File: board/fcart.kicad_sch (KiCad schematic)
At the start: 110 parts, among them J1 USB4085, J2 MSD-4-A, J3 SWD, J4 JTAG, J5 Famicom_cartridge, Q1 DTC114E, SW1 PTS647SM70, U1 USBLC6-2SC6, U10 W9864G6KH-6, U2 TLV76133DCY, U3 MCP6001, U4 SN74ALVC164245DGG, U5 SN74ALVC164245DGG, U6 SN74ALVC164245DGG, U7 SN74ALVC164245DGG, U8 STM32F412RET6, U9 LCMXO2-4000HC-4TG144C, Y1 ABS07-32.768KHZ-7, Y2 ABM8W-12.0000MHZ-8-B1U, Y3 ASE-50.000MHZ-LC

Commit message: pcb: Fix USB backpowering to the console through level shifters
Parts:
- removed C14: 47u, Capacitor_SMD:C_1206_3216Metric, symbol Device:C
- removed C4: 10u, Capacitor_SMD:C_0805_2012Metric, symbol Device:C
- removed D1, D2: MBR120, Diode_SMD:D_SOD-123F, symbol Device:D_Schottky
- added C15, C20, C3, C58: 10u, Capacitor_SMD:C_0805_2012Metric, symbol Device:C
- added C5: 0.1u, Capacitor_SMD:C_0805_2012Metric, symbol Device:C
- added JP2: CLONE FIX, Jumper:SolderJumper-2_P1.3mm_Bridged_RoundedPad1.0x1.5mm, symbol Jumper:SolderJumper_2_Bridged
- added R16, R17: 1k, Resistor_SMD:R_0805_2012Metric, symbol Device:R
- added R3: 100k, Resistor_SMD:R_0805_2012Metric, symbol Device:R
- added U2, U3: LM66100DCK, Package_TO_SOT_SMD:SOT-363_SC-70-6, symbol Power_Management:LM66100DCK
- JP1: value SND-IN-OUT -> NO EXP SND
- Q1: value DTC114E -> DTC114EK
- R19: renamed from R5; value 10k -> 5.1k
- U11: renamed from U9; value LCMXO2-4000HC-4TG144C -> LCMXO2-4000HC-4TG144
- U6: renamed from U4; value SN74ALVC164245DGG -> SN74LVC16T245D
- U7: renamed from U5; value SN74ALVC164245DGG -> SN74LVC16T245D
- U8: renamed from U6; value SN74ALVC164245DGG -> SN74LVC16T245D
- U9: renamed from U7; value SN74ALVC164245DGG -> SN74LVC16T245D
- renumbered C5 to C1, C9 to C10, C10 to C11, C11 to C12, C12 to C13, C13 to C14, C15 to C16, C16 to C17, C17 to C18, C18 to C19, C3 to C2, C19 to C21, C20 to C22, C21 to C23, C22 to C24, C23 to C25, C24 to C26, C25 to C27, C26 to C28, C27 to C29, C28 to C30, C29 to C31, C30 to C32, C31 to C33, C32 to C34, C33 to C35, C34 to C36, C35 to C37, C36 to C38, C37 to C39, C1 to C4, C38 to C40, C39 to C41, C40 to C42, C41 to C43, C42 to C44, C43 to C45, C44 to C46, C45 to C47, C46 to C48, C47 to C49, C48 to C50, C49 to C51, C50 to C52, C51 to C53, C52 to C54, C53 to C55, C54 to C56, C55 to C57, C2 to C6, C6 to C7, C7 to C8, C8 to C9, D3 to D1, R16 to R18, R17 to R20, R3 to R4, R4 to R5, U8 to U10, U10 to U12, U2 to U4, U3 to U5
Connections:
- net +3V3: now also C20.1, C58.1
- net +5V: now also C5.1, U2.6 (VOUT), U3.6 (VOUT)
- net CIRAM_A10: now also U11.68 (PB29A/BANK2/T), U8.47 (1A0); no longer U11.67 (PB27B/BANK2/C), U8.46 (1A1)
- net CIRAM_A10_5V: now also RN7.7 (R2.2); no longer U8.3 (1B1)
- net CIRAM_CE: now also U11.69 (PB29B/BANK2/C), U8.46 (1A1); no longer U11.68 (PB29A/BANK2/T), U8.44 (1A2)
- net CIRAM_CE_5V: now also RN7.8 (R1.2); no longer U8.5 (1B2)
- net GND: now also U8.44 (1A2), C20.2, C3.2, C5.2, C58.2, R17.1, R3.1, U2.2 (GND), U2.5 (ST), U3.2 (GND), U3.5 (ST)
- net IRQ: now also Q1.1 (B); no longer U8.47 (1A0)
- net IRQ_5V: now also Q1.3 (C); no longer U8.2 (1B0)
- net LS_OE: now also U11.67 (PB27B/BANK2/C); no longer Q1.3 (C)
- net PPU_A0: now also U11.89 (PR10C/BANK1/T); no longer U11.87 (PR10D/BANK1/C)
- net PPU_A1: now also U11.86 (PR13A/BANK1/T/DQS1); no longer U11.85 (PR13B/BANK1/C/DQS1N)
- net PPU_A10: now also U11.83 (PR14B/BANK1/C/DQ1); no longer U11.82 (PR15A/BANK1/T/DQ1)
- net PPU_A11: now also U11.85 (PR13B/BANK1/C/DQS1N); no longer U11.84 (PR14A/BANK1/T/DQ1)
- net PPU_A12: now also U11.87 (PR10D/BANK1/C); no longer U11.86 (PR13A/BANK1/T/DQS1)
- net PPU_A13: now also U11.91 (PR10B/BANK1/C/PCLKC1_0/DQ0); no longer U11.89 (PR10C/BANK1/T)
- net PPU_A2: now also U11.84 (PR14A/BANK1/T/DQ1); no longer U11.83 (PR14B/BANK1/C/DQ1)
- net PPU_A3: now also U11.82 (PR15A/BANK1/T/DQ1); no longer U11.81 (PR15B/BANK1/C/DQ1)
- net PPU_A4: now also U11.78 (PR16A/BANK1/T/DQ1); no longer U11.77 (PR16B/BANK1/C/DQ1)
- net PPU_A5: now also U11.76 (PR18A/BANK1/T/DQ1); no longer U11.75 (PR18B/BANK1/C/DQ1)
- net PPU_A6: now also U11.74 (PR19A/BANK1/T/DQ1); no longer U11.73 (PR19B/BANK1/C/DQ1)
- net PPU_A7: now also U11.75 (PR18B/BANK1/C/DQ1); no longer U11.74 (PR19A/BANK1/T/DQ1)
- net PPU_A8: now also U11.77 (PR16B/BANK1/C/DQ1); no longer U11.76 (PR18A/BANK1/T/DQ1)
- net PPU_A9: now also U11.81 (PR15B/BANK1/C/DQ1); no longer U11.78 (PR16A/BANK1/T/DQ1)
- net PPU_D0: now also U11.92 (PR10A/BANK1/T/PCLKT1_0/DQ0); no longer U11.91 (PR10B/BANK1/C/PCLKC1_0/DQ0)
- net PPU_D1: now also U11.94 (PR9A/BANK1/T/DQS0); no longer U11.93 (PR9B/BANK1/C/DQS0N)
- net PPU_D2: now also U11.96 (PR8A/BANK1/T/DQ0); no longer U11.95 (PR8B/BANK1/C/DQ0)
- net PPU_D3: now also U11.98 (PR6A/BANK1/T/DQ0); no longer U11.97 (PR6B/BANK1/C/DQ0)
- net PPU_D4: now also U11.99 (PR5B/BANK1/C/DQ0); no longer U11.98 (PR6A/BANK1/T/DQ0)
- net PPU_D5: now also U11.97 (PR6B/BANK1/C/DQ0); no longer U11.96 (PR8A/BANK1/T/DQ0)
- net PPU_D6: now also U11.95 (PR8B/BANK1/C/DQ0); no longer U11.94 (PR9A/BANK1/T/DQS0)
- net PPU_D7: now also U11.93 (PR9B/BANK1/C/DQS0N); no longer U11.92 (PR10A/BANK1/T/PCLKT1_0/DQ0)
- net PPU_DIR: now also U11.100 (PR5A/BANK1/T/DQ0); no longer U11.99 (PR5B/BANK1/C/DQ0)
- net PPU_WR: now also U11.73 (PR19B/BANK1/C/DQ1); no longer U11.69 (PB29B/BANK2/C)
- net SND_OUT: now also C15.2
- net VCART: now also C3.1, R16.2, R3.2, U2.3 (~{CE}), U3.1 (VIN); no longer Q1.1 (B)
- net VUSB: now also U2.1 (VIN), U3.3 (~{CE})
- net at C14.2, R14.1, U5.1: now also C15.1
- net at RN7.1 (R1.1): now also JP2.1 (A)
- net at RN7.2 (R2.1): now also U8.2 (1B0)
- net at J5.49 (PPU_~{A13}): now also R16.1, R17.2
- new net: JP2.2 (B), U8.3 (1B1)
- no-connect marks 46 -> 41
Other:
- moved on the sheet: BT1, C1, C10, C11, C12, C13, C14, C16, C17, C2, C4, C41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

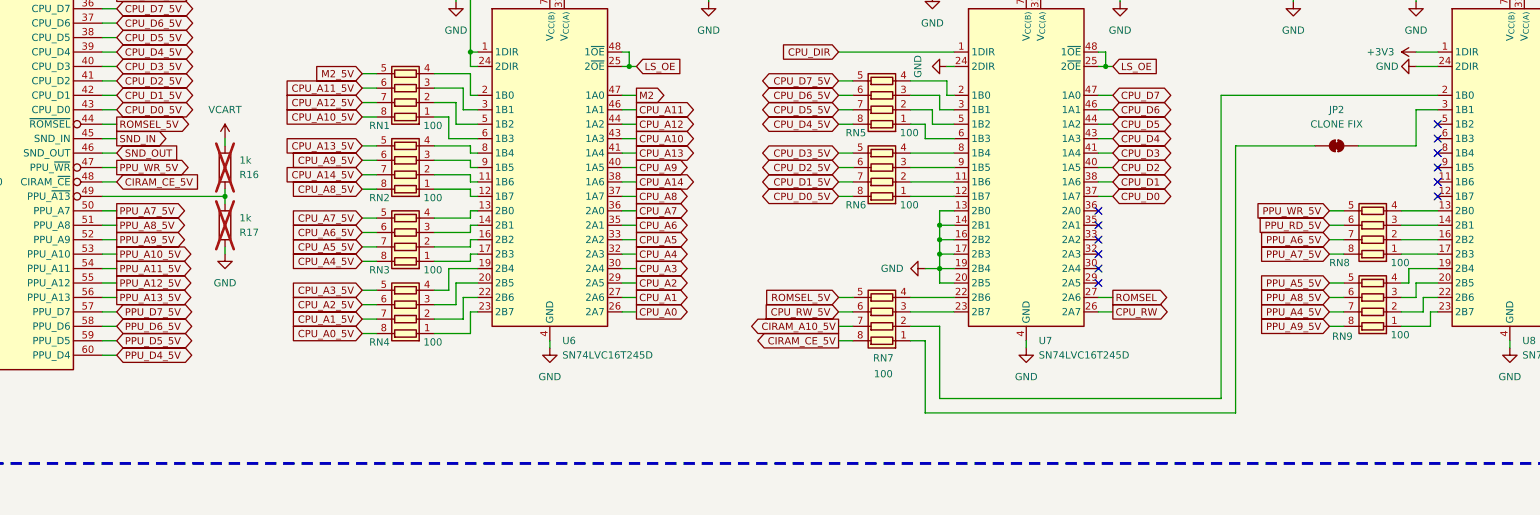
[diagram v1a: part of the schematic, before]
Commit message: hw: rework signal assignments for new PCB rev
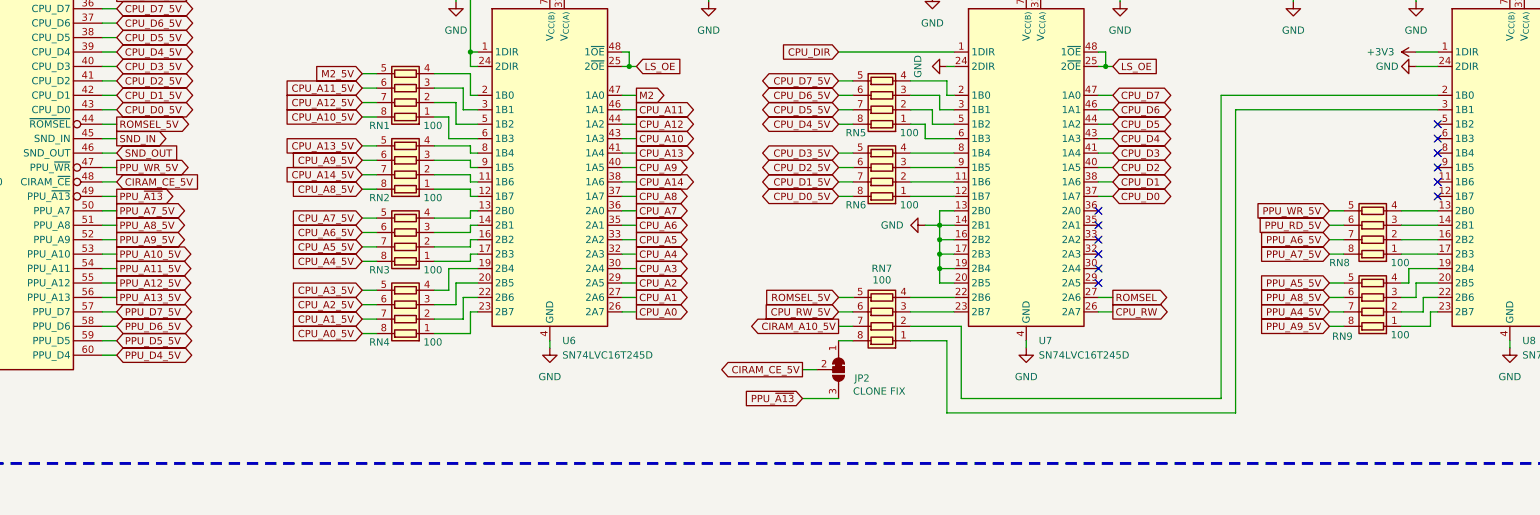
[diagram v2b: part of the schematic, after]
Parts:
- removed JP2: CLONE FIX, Jumper:SolderJumper-2_P1.3mm_Bridged_RoundedPad1.0x1.5mm, symbol Jumper:SolderJumper_2_Bridged
- removed R16, R17: 1k, Resistor_SMD:R_0805_2012Metric, symbol Device:R
- added JP2: CLONE FIX, Jumper:SolderJumper-3_P1.3mm_Bridged12_RoundedPad1.0x1.5mm, symbol Jumper:SolderJumper_3_Bridged12
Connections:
- net CIRAM_CE_5V: now also JP2.2 (C); no longer RN7.8 (R1.2)
- net PPU_~{A13}: now reaches J5.49 (PPU_~{A13})
- net PPU_~{A13}: now also JP2.3 (B)
- net at RN7.1 (R1.1): now also U8.3 (1B1)
- new net: JP2.1 (A), RN7.8 (R1.2)

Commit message: ci: automate generation of KiCad manufacturing files
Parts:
- BT1: DigiKey (none) -> 36-1060CT-ND; LCSC (none) -> C238069
- C1, C18, C19: DigiKey (none) -> 311-1140-1-ND; LCSC (none) -> C49678
- C10: renamed from C8; DigiKey (none) -> 1276-2873-1-ND; LCSC (none) -> C107365
- C11: renamed from C9; DigiKey (none) -> 13-CC0805KPX7R0BB103CT-ND; LCSC (none) -> C83170
- C12: renamed from C10; DigiKey (none) -> 1276-2873-1-ND; LCSC (none) -> C107365
- C13: renamed from C11; DigiKey (none) -> 1276-2873-1-ND; LCSC (none) -> C107365
- C14: renamed from C12; DigiKey (none) -> 1276-2873-1-ND; LCSC (none) -> C107365
- C15: renamed from C13; DigiKey (none) -> 311-1140-1-ND; LCSC (none) -> C49678
- C16: renamed from C14; DigiKey (none) -> 311-1831-1-ND; LCSC (none) -> C519942
- C17: renamed from C15; DigiKey (none) -> 1276-1096-1-ND; LCSC (none) -> C1713
- C2: renamed from C4; DigiKey (none) -> 1276-1096-1-ND; LCSC (none) -> C1713
- C20: renamed from C21; DigiKey (none) -> 311-1140-1-ND; LCSC (none) -> C49678
- C21: renamed from C22; DigiKey (none) -> 311-1140-1-ND; LCSC (none) -> C49678
- C22: renamed from C23; DigiKey (none) -> 311-1140-1-ND; LCSC (none) -> C49678
- C23: renamed from C24; DigiKey (none) -> 311-1140-1-ND; LCSC (none) -> C49678
- C24: renamed from C25; DigiKey (none) -> 311-1140-1-ND; LCSC (none) -> C49678
- C25: renamed from C26; DigiKey (none) -> 311-1140-1-ND; LCSC (none) -> C49678
- C26: renamed from C27; DigiKey (none) -> 311-1831-1-ND; LCSC (none) -> C519942
- C27: renamed from C28; DigiKey (none) -> 311-1831-1-ND; LCSC (none) -> C519942
- C28: renamed from C29; DigiKey (none) -> 311-1140-1-ND; LCSC (none) -> C49678
- C29: renamed from C16; DigiKey (none) -> 311-1831-1-ND; LCSC (none) -> C519942
- C3: renamed from C5; DigiKey (none) -> 311-1140-1-ND; LCSC (none) -> C49678
- C30: renamed from C17; DigiKey (none) -> 311-1831-1-ND; LCSC (none) -> C519942
- C31: renamed from C30; DigiKey (none) -> 311-1140-1-ND; LCSC (none) -> C49678
- C32: renamed from C31; DigiKey (none) -> 311-1140-1-ND; LCSC (none) -> C49678
- C33: renamed from C32; DigiKey (none) -> 1276-2873-1-ND; LCSC (none) -> C107365
- C34: renamed from C33; DigiKey (none) -> 311-1140-1-ND; LCSC (none) -> C49678
- C35: renamed from C34; DigiKey (none) -> 311-1140-1-ND; LCSC (none) -> C49678
- C36: renamed from C35; DigiKey (none) -> 311-1140-1-ND; LCSC (none) -> C49678
- C37: renamed from C36; DigiKey (none) -> 311-1140-1-ND; LCSC (none) -> C49678
- C38: renamed from C37; DigiKey (none) -> 311-1140-1-ND; LCSC (none) -> C49678
- C39: renamed from C38; DigiKey (none) -> 311-1140-1-ND; LCSC (none) -> C49678
- C4: renamed from C2; DigiKey (none) -> 1276-1096-1-ND; LCSC (none) -> C1713
- C40: renamed from C39; DigiKey (none) -> 311-1140-1-ND; LCSC (none) -> C49678
- C41: renamed from C40; DigiKey (none) -> 311-1140-1-ND; LCSC (none) -> C49678
- C42: renamed from C41; DigiKey (none) -> 311-1140-1-ND; LCSC (none) -> C49678
- C43: renamed from C42; DigiKey (none) -> 311-1140-1-ND; LCSC (none) -> C49678
- C44: renamed from C43; DigiKey (none) -> 311-1140-1-ND; LCSC (none) -> C49678
- C45: renamed from C44; DigiKey (none) -> 311-1140-1-ND; LCSC (none) -> C49678
- C46: renamed from C45; DigiKey (none) -> 311-1140-1-ND; LCSC (none) -> C49678
- C47: renamed from C46; DigiKey (none) -> 311-1140-1-ND; LCSC (none) -> C49678
- C48: renamed from C47; DigiKey (none) -> 311-1140-1-ND; LCSC (none) -> C49678
- C49: renamed from C48; DigiKey (none) -> 311-1140-1-ND; LCSC (none) -> C49678
- C5: renamed from C3; DigiKey (none) -> 1276-1096-1-ND; LCSC (none) -> C1713
- C50: renamed from C49; DigiKey (none) -> 311-1140-1-ND; LCSC (none) -> C49678
- C51: renamed from C50; DigiKey (none) -> 311-1140-1-ND; LCSC (none) -> C49678
- C52: renamed from C51; DigiKey (none) -> 311-1140-1-ND; LCSC (none) -> C49678
- C53: renamed from C52; DigiKey (none) -> 311-1140-1-ND; LCSC (none) -> C49678
- C54: renamed from C53; DigiKey (none) -> 311-1140-1-ND; LCSC (none) -> C49678
- C55: renamed from C54; DigiKey (none) -> 311-1140-1-ND; LCSC (none) -> C49678
- C56: renamed from C55; DigiKey (none) -> 311-1140-1-ND; LCSC (none) -> C49678
- C57: renamed from C56; DigiKey (none) -> 311-1140-1-ND; LCSC (none) -> C49678
- C58: renamed from C57; DigiKey (none) -> 311-1140-1-ND; LCSC (none) -> C49678
- C6: DigiKey (none) -> 1276-1096-1-ND; LCSC (none) -> C1713
- C7: renamed from C20; DigiKey (none) -> 1276-1096-1-ND; LCSC (none) -> C1713
- C8: renamed from C58; DigiKey (none) -> 1276-1096-1-ND; LCSC (none) -> C1713
- C9: renamed from C7; DigiKey (none) -> 311-1140-1-ND; LCSC (none) -> C49678
- D1: footprint fcart:LED_1208_Horizontal_3210Metric -> hiot:LED_1208_Horizontal_3210Metric; DigiKey (none) -> 160-LTST-S321KRKTCT-ND; LCSC (none) -> C6897245
- J1: DigiKey (none) -> 2073-USB4085-GF-ACT-ND; LCSC (none) -> C7095263
- J2: footprint fcart:microSD_HC_Same_Sky_MSD-4-A -> hiot:microSD_HC_Same_Sky_MSD-4-A; DigiKey (none) -> 2223-MSD-4-ACT-ND; LCSC (none) -> C5155563
- J5: footprint fcart:Famicom cartridge pcb -> hiot:Famicom cartridge pcb; symbol fcart:Famicom_cartridge -> hiot:Famicom_cartridge
- Q1: DigiKey (none) -> DTC114EKAT146CT-ND; LCSC (none) -> C79971
- R1, R11, R2, R8: DigiKey (none) -> 311-5.10KCRCT-ND; LCSC (none) -> C84375
- R10, R14, R15, R6: DigiKey (none) -> 311-10.0KCRCT-ND; LCSC (none) -> C140868
- R12, R13: DigiKey (none) -> 311-100KCRCT-ND; LCSC (none) -> C96346
- R16: renamed from R18; DigiKey (none) -> 311-10.0KCRCT-ND; LCSC (none) -> C140868
- R17: renamed from R19; DigiKey (none) -> 311-5.10KCRCT-ND; LCSC (none) -> C84375
- R18: renamed from R20; DigiKey (none) -> 311-10.0KCRCT-ND; LCSC (none) -> C140868
- R3: renamed from R4; DigiKey (none) -> 311-5.10KCRCT-ND; LCSC (none) -> C84375
- R4: renamed from R5; DigiKey (none) -> 311-10.0KCRCT-ND; LCSC (none) -> C140868
- R5: renamed from R3; DigiKey (none) -> 311-100KCRCT-ND; LCSC (none) -> C96346
- R7, R9: DigiKey (none) -> 311-1.00KCRCT-ND; LCSC (none) -> C95781
- RN1, RN10, RN11, RN12, RN13, RN2, RN3, RN4, RN5, RN6, RN7, RN8, RN9: DigiKey (none) -> YC124J-100CT-ND; LCSC (none) -> C79203
- SW1: DigiKey (none) -> 108-PTS647SM70SMTR2LFSCT-ND; LCSC (none) -> C2689517
- U1: DigiKey (none) -> 497-5235-1-ND; LCSC (none) -> C2827654
- U10: DigiKey (none) -> 497-18546-ND; LCSC (none) -> C89374
- U11: DigiKey (none) -> 220-1460-ND; LCSC (none) -> C1521625
- U12: DigiKey (none) -> W9864G6KH-6-ND; LCSC (none) -> C62378
- U2, U3: DigiKey (none) -> 296-53541-1-ND; LCSC (none) -> C2869734
- U4: DigiKey (none) -> 296-TLV76133DCYRCT-ND; LCSC (none) -> C7527500
- U5: DigiKey (none) -> MCP6001T-I/OTCT-ND; LCSC (none) -> C116490
- U6, U7, U8, U9: DigiKey (none) -> 296-20631-1-ND; LCSC (none) -> C148170
- Y1: renamed from Y2; DigiKey (none) -> 535-14008-1-ND; LCSC (none) -> C1985372
- Y2: renamed from Y1; DigiKey (none) -> 535-9543-1-ND; LCSC (none) -> C276424
- Y3: DigiKey (none) -> 535-ASE-50.000MHZ-L-C-TCT-ND; LCSC (none) -> C596955
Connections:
- net FPGA_IRQ: now also U10.62 (PB9), U11.113 (PT25B/BANK0/C/LVDS); no longer U10.20 (PA4), U11.111 (PT27B/BANK0/C/LVDS)
- net GND: now also J1.SH (SHIELD), J2.SH (SHIELD); no longer J1.S1 (SHIELD), J2.10 (SHIELD)
- net LED: now also U10.59 (PB7); no longer U10.58 (PB6)
- net QSPI_IO0: now also U10.40 (PC9), U11.111 (PT27B/BANK0/C/LVDS); no longer U10.22 (PA6), U11.112 (PT27A/BANK0/T/LVDS)
- net QSPI_IO1: now also U10.51 (PC10), U11.110 (PT28C/BANK0/T/INITN); no longer U10.23 (PA7), U11.113 (PT25B/BANK0/C/LVDS)
- net QSPI_IO2: now also U10.39 (PC8); no longer U10.24 (PC4)
- net QSPI_IO3: now also U10.15 (PA1); no longer U10.25 (PC5)
- net QSPI_NCS: now also U10.58 (PB6), U11.112 (PT27A/BANK0/T/LVDS); no longer U10.52 (PC11), U11.110 (PT28C/BANK0/T/INITN)
- net SD_DAT1: now also U10.41 (PA8); no longer U10.40 (PC9)
- net SD_DAT2: now also U10.42 (PA9); no longer U10.51 (PC10)
- net SPI_MISO: now also U10.22 (PA6); no longer U10.10 (PC2)
- net SPI_MOSI: now also U10.23 (PA7); no longer U10.11 (PC3)
- net SPI_NCS: now also U10.17 (PA3); no longer U10.16 (PA2)
- net SPI_SCK: now also U10.21 (PA5); no longer U10.38 (PC7)
- net USB_DET: now also U10.26 (PB0); no longer U10.42 (PA9)
- net OSC32_IN: no longer names the net of C29.2, U10.3 (PC14), Y2.2
- net OSC32_OUT: no longer names the net of C30.2, U10.4 (PC15), Y2.1
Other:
- moved on the sheet: BT1, C1, C10, C11, C12, C13, C14, C15, C16, C17, C2, C29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
